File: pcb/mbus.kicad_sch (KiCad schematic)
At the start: 27 parts, among them Q1 Q_NPN_BEC_BRT, Q3 Q_NPN_BEC_BRT

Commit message: Manufactured board
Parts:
- removed Q1, Q3: Q_NPN_BEC_BRT, Package_TO_SOT_SMD:SOT-23, symbol Device:Q_NPN_BEC_BRT
- added Q1, Q3: BC846, Package_TO_SOT_SMD:SOT-23, symbol Transistor_BJT:BC846
- added R47: 5K1, Resistor_SMD:R_0402_1005Metric, symbol Device:R
- C?: LCSC (none) -> C1523
- R43: value 20K -> 10K; LCSC C25765 -> C25744
- R? (x2): value 47K -> 10K; LCSC (none) -> C25744
- R?: value 47K -> 20K; LCSC (none) -> C25765
- R?: LCSC (none) -> C17408
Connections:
- net +36V: now also Q?.2 (S), R47.2; no longer Q?.3 (D), R?.1
- net GND: now also Q1.2 (E), Q3.2 (E)
- net Rx: now also Q3.3 (C)
- net Tx: now also Q1.1 (B)
- net at Q?.1 (G): now also R?.1, R47.1; no longer R?.2
- net at R?.2, U?.7: now also Q3.1 (B)
- net at D?.1 (K), D?.2 (A): now also Q?.3 (D); no longer Q?.2 (S)
- new net: Q1.3 (C), R?.2
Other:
- moved on the sheet: D?, Q?, R?

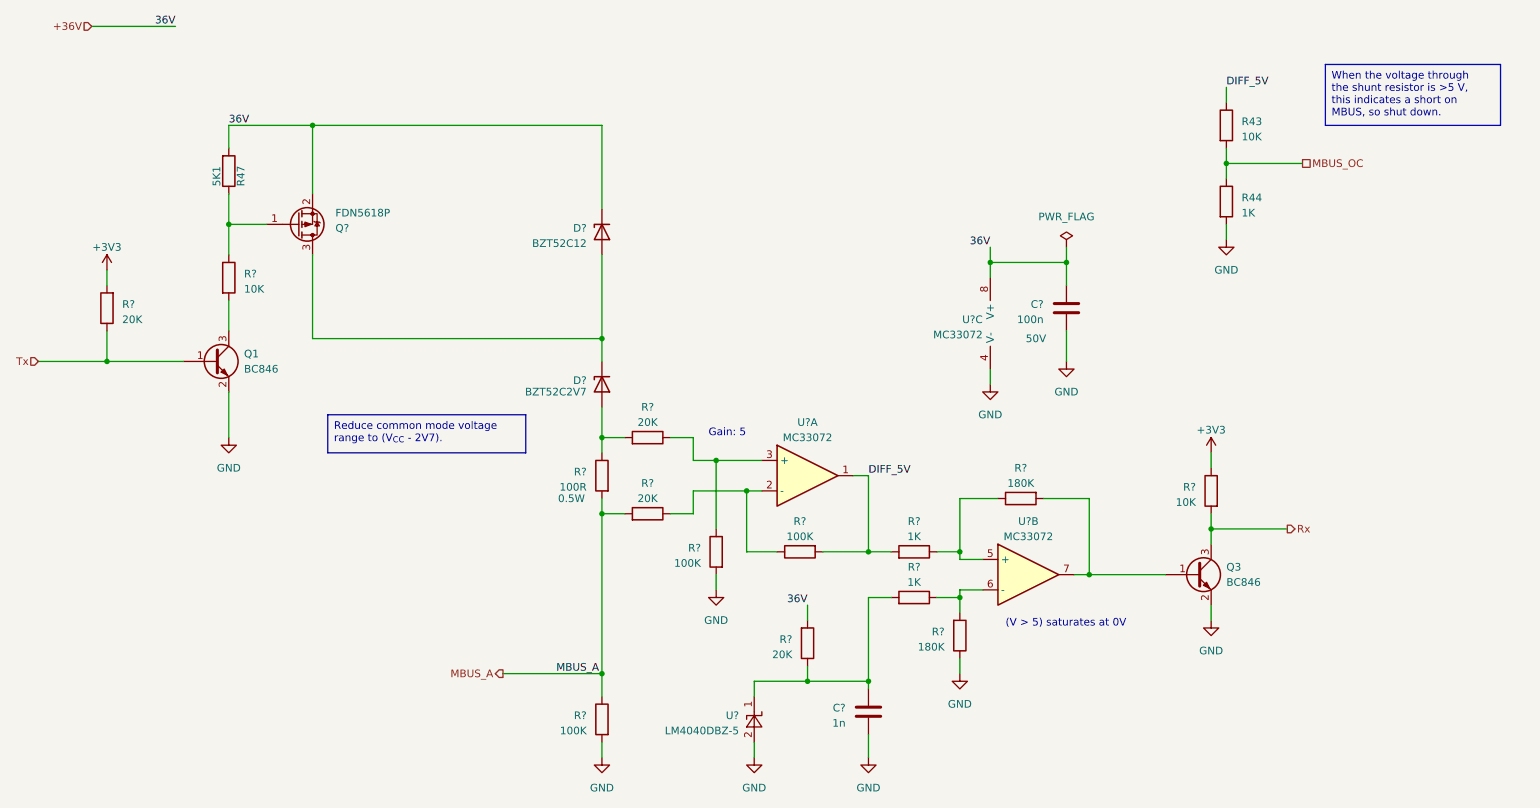
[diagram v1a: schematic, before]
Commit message: emonHP with Pi attachment
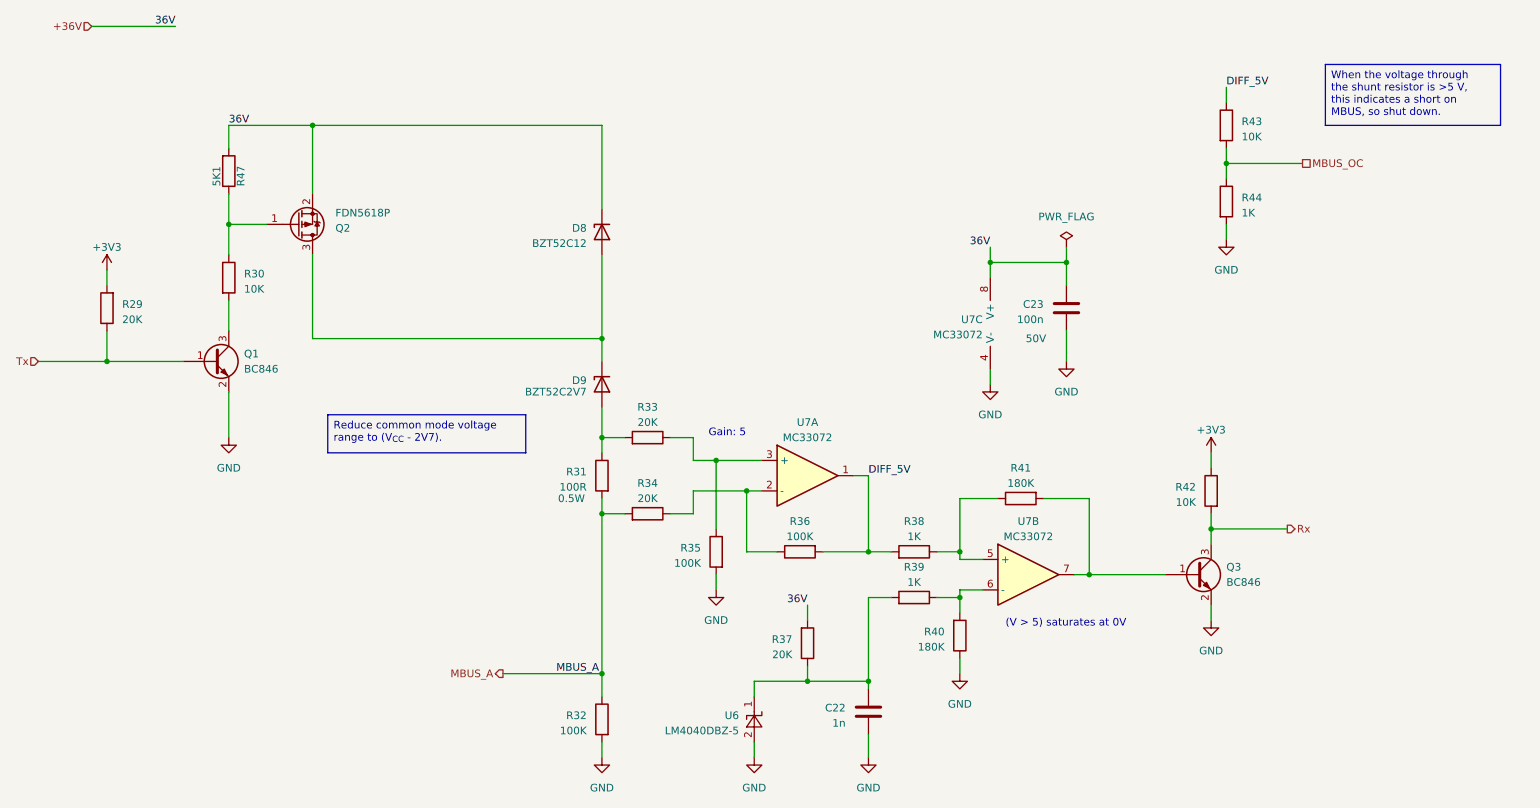
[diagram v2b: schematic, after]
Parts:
- gave numbers to parts that had none: 21
